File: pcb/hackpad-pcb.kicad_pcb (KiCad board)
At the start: 2 copper layers, 33 parts, among them U1 MCU_Seeed_XIAO_RP2040

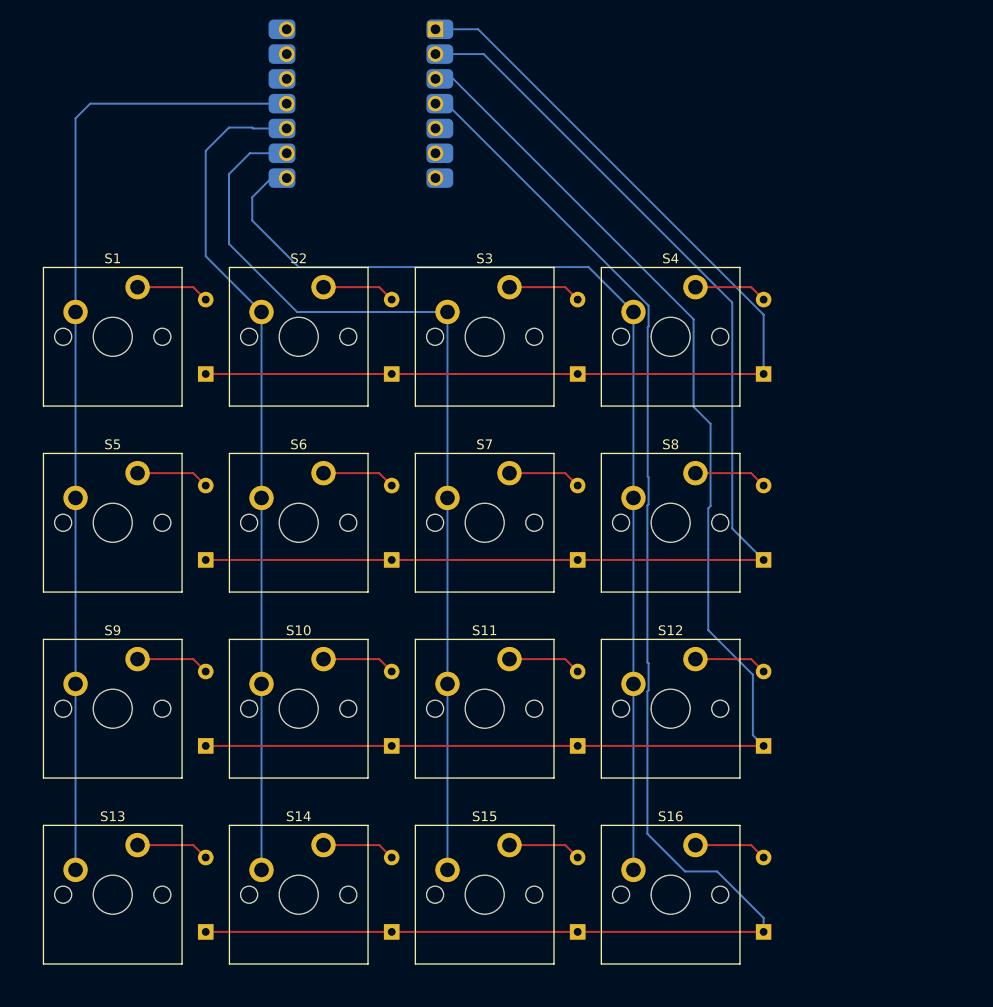
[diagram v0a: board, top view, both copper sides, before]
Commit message: Moved diodes and added OLED
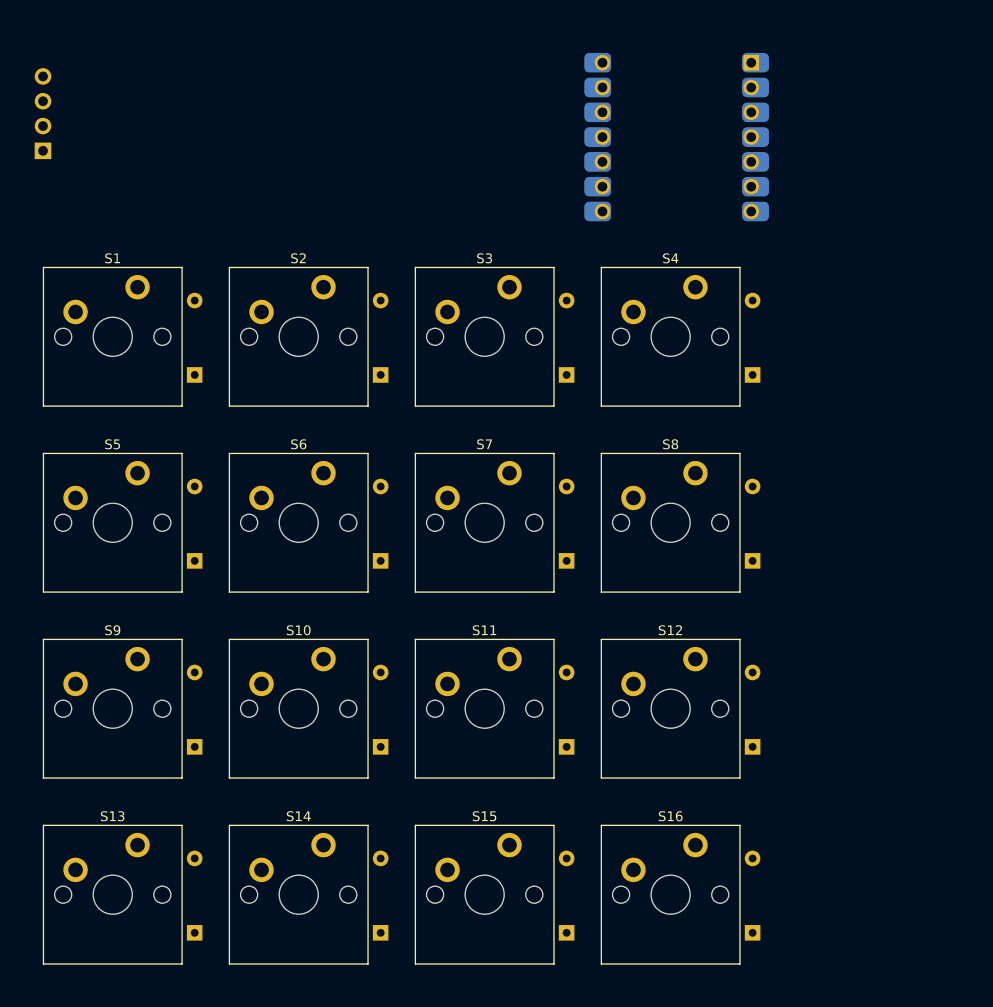
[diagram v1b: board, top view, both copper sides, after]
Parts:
- added J1: OLED_128x32, ScottoKeebs_Components:OLED_128x32, F.Cu at (105.6, 47.4)
- moved U1 32.5 mm to (172.1, 55.7)
- moved D11 1.14 mm to (160.8, 118.2)
- moved D15 1.14 mm to (160.8, 137.3)
- moved D3 1.14 mm to (160.8, 80.1)
- moved D7 1.14 mm to (160.8, 99.2)
- moved D1 1.14 mm to (122.7, 80.1)
- moved D13 1.14 mm to (122.7, 137.3)
- moved D5 1.14 mm to (122.7, 99.2)
- moved D9 1.14 mm to (122.7, 118.2)
- moved D10 1.14 mm to (141.7, 118.2)
- moved D12 1.14 mm to (179.8, 118.2)
- moved D14 1.14 mm to (141.7, 137.3)
- moved D16 1.14 mm to (179.8, 137.3)
- moved D2 1.14 mm to (141.7, 80.1)
- moved D4 1.14 mm to (179.8, 80.1)
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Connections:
- U1 pad 13: unconnected-(U1-GND-Pad13) -> GND
- U1 pad 14: unconnected-(U1-5V-Pad14) -> VCC
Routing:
- net Row 3: track 158.8 -> 0.00 mm
- net Row 2: track 140.2 -> 0.00 mm
- net Row 1: track 125.3 -> 0.00 mm
- net Row 0: track 108.9 -> 0.00 mm
- net Column 3: track 106.3 -> 0.00 mm
- net Column 0: track 98.8 -> 0.00 mm
- net Column 2: track 96.4 -> 0.00 mm
- net Column 1: track 84.9 -> 0.00 mm
- net Net-(D7-A): track 7.51 -> 0.00 mm
- net Net-(D6-A): track 7.51 -> 0.00 mm
- net Net-(D3-A): track 7.51 -> 0.00 mm
- net Net-(D2-A): track 7.51 -> 0.00 mm
- net Net-(D11-A): track 7.51 -> 0.00 mm
- net Net-(D10-A): track 7.51 -> 0.00 mm
- net Net-(D9-A): track 7.51 -> 0.00 mm
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
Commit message: Routed a little bit more
Signed-off-by: Urjith Mishra <66270347+TheScientist101@users.noreply.github.com>
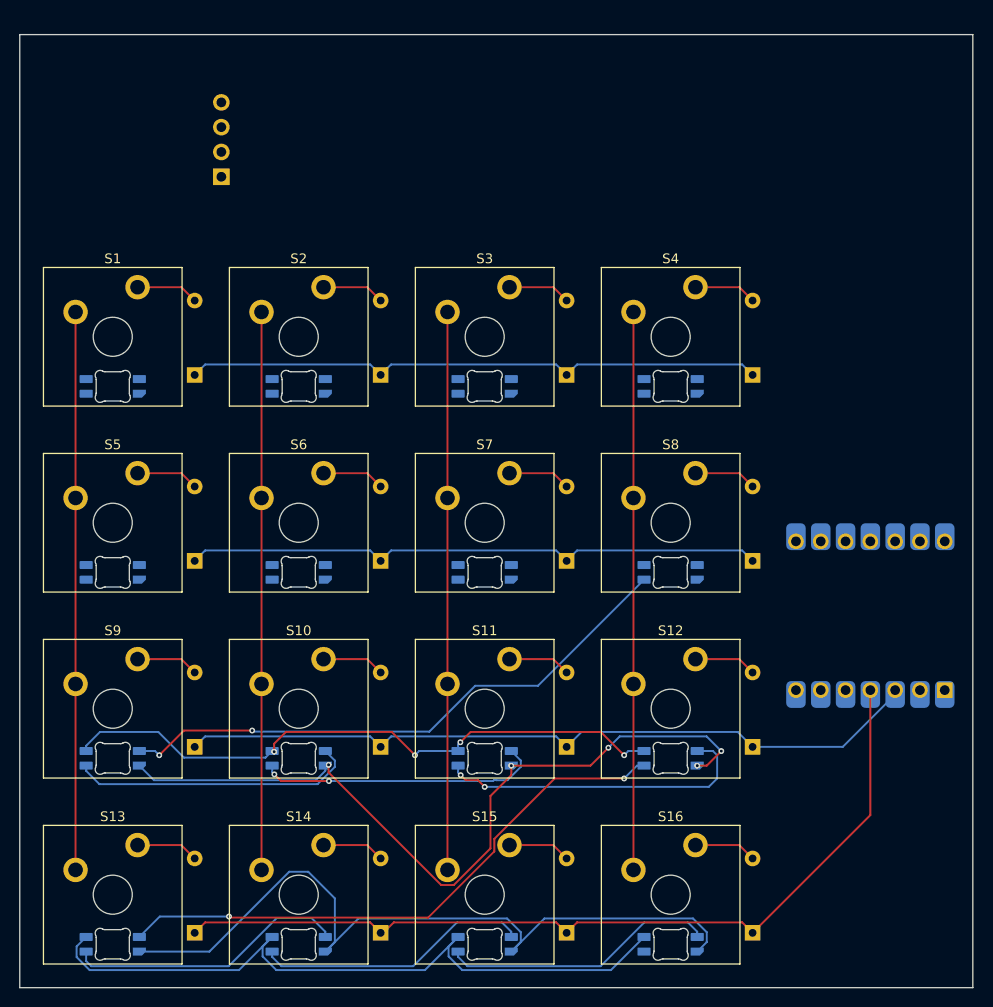
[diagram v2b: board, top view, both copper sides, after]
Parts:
- added LED1: MX_SK6812MINI-E, PCM_marbastlib-mx:LED_MX_6028R, B.Cu at (114.3, 81.3)
- added LED10: MX_SK6812MINI-E, PCM_marbastlib-mx:LED_MX_6028R, B.Cu at (133.3, 119.4)
- added LED11: MX_SK6812MINI-E, PCM_marbastlib-mx:LED_MX_6028R, B.Cu at (152.4, 119.4)
- added LED12: MX_SK6812MINI-E, PCM_marbastlib-mx:LED_MX_6028R, B.Cu at (171.4, 119.4)
- added LED13: MX_SK6812MINI-E, PCM_marbastlib-mx:LED_MX_6028R, B.Cu at (114.3, 138.4)
- added LED14: MX_SK6812MINI-E, PCM_marbastlib-mx:LED_MX_6028R, B.Cu at (133.3, 138.4)
- added LED15: MX_SK6812MINI-E, PCM_marbastlib-mx:LED_MX_6028R, B.Cu at (152.4, 138.4)
- added LED16: MX_SK6812MINI-E, PCM_marbastlib-mx:LED_MX_6028R, B.Cu at (171.4, 138.4)
- added LED2: MX_SK6812MINI-E, PCM_marbastlib-mx:LED_MX_6028R, B.Cu at (133.3, 81.3)
- added LED3: MX_SK6812MINI-E, PCM_marbastlib-mx:LED_MX_6028R, B.Cu at (152.4, 81.3)
- added LED4: MX_SK6812MINI-E, PCM_marbastlib-mx:LED_MX_6028R, B.Cu at (171.4, 81.3)
- added LED5: MX_SK6812MINI-E, PCM_marbastlib-mx:LED_MX_6028R, B.Cu at (114.3, 100.3)
- added LED6: MX_SK6812MINI-E, PCM_marbastlib-mx:LED_MX_6028R, B.Cu at (133.3, 100.3)
- added LED7: MX_SK6812MINI-E, PCM_marbastlib-mx:LED_MX_6028R, B.Cu at (152.4, 100.3)
- added LED8: MX_SK6812MINI-E, PCM_marbastlib-mx:LED_MX_6028R, B.Cu at (171.4, 100.3)
- added LED9: MX_SK6812MINI-E, PCM_marbastlib-mx:LED_MX_6028R, B.Cu at (114.3, 119.4)
- S1, S10, S11, S12, S13, S14, S15, S16, S2, S3, S4, S5, S6, S7, S8, S9: footprint ScottoKeebs_MX:MX_PCB_1.00u -> ScottoKeebs_MX:MX_Plate_1.00u
- moved U1 52.9 mm to (191.9, 104.8), turned to 90 degrees
- moved J1 18.5 mm to (123.8, 50.0)
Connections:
- J1 pad 3: unconnected-(J1-SCL-Pad3) -> /SCL
- J1 pad 4: unconnected-(J1-SDA-Pad4) -> /SDA
- U1 pad 5: unconnected-(U1-PA8_A4_D4_SDA-Pad5) -> /SDA
- U1 pad 6: unconnected-(U1-PA9_A5_D5_SCL-Pad6) -> /SCL
- U1 pad 7: unconnected-(U1-PB08_A6_D6_TX-Pad7) -> /LED Connector 0
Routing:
- net GND: track 0.00 -> 159.7 mm, vias 0 -> 5
- net VCC: track 0.00 -> 137.8 mm, vias 0 -> 4
- net Row 3: track 0.00 -> 89.7 mm
- net Row 2: track 0.00 -> 77.0 mm
- net /LED Connector 3: track 0.00 -> 59.8 mm, vias 0 -> 2
- net Row 0: track 0.00 -> 59.8 mm
- net Row 1: track 0.00 -> 59.8 mm
- net /LED Connector 2: track 0.00 -> 59.4 mm, vias 0 -> 2
- net Column 3: track 0.00 -> 57.2 mm
- net Column 2: track 0.00 -> 57.2 mm
- net Column 1: track 0.00 -> 57.2 mm
- net Column 0: track 0.00 -> 57.2 mm
- net Net-(LED11-DOUT): track 0.00 -> 32.8 mm, vias 0 -> 2
- net Net-(LED10-DIN): track 0.00 -> 30.1 mm
- net Net-(LED10-DOUT): track 0.00 -> 29.2 mm, vias 0 -> 2
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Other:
- board outline added: 97.6 x 97.6 mm

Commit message: Replaced neopixels with simple 2x3x4 mm leds to avoid smd soldering
Signed-off-by: Urjith Mishra <66270347+TheScientist101@users.noreply.github.com>
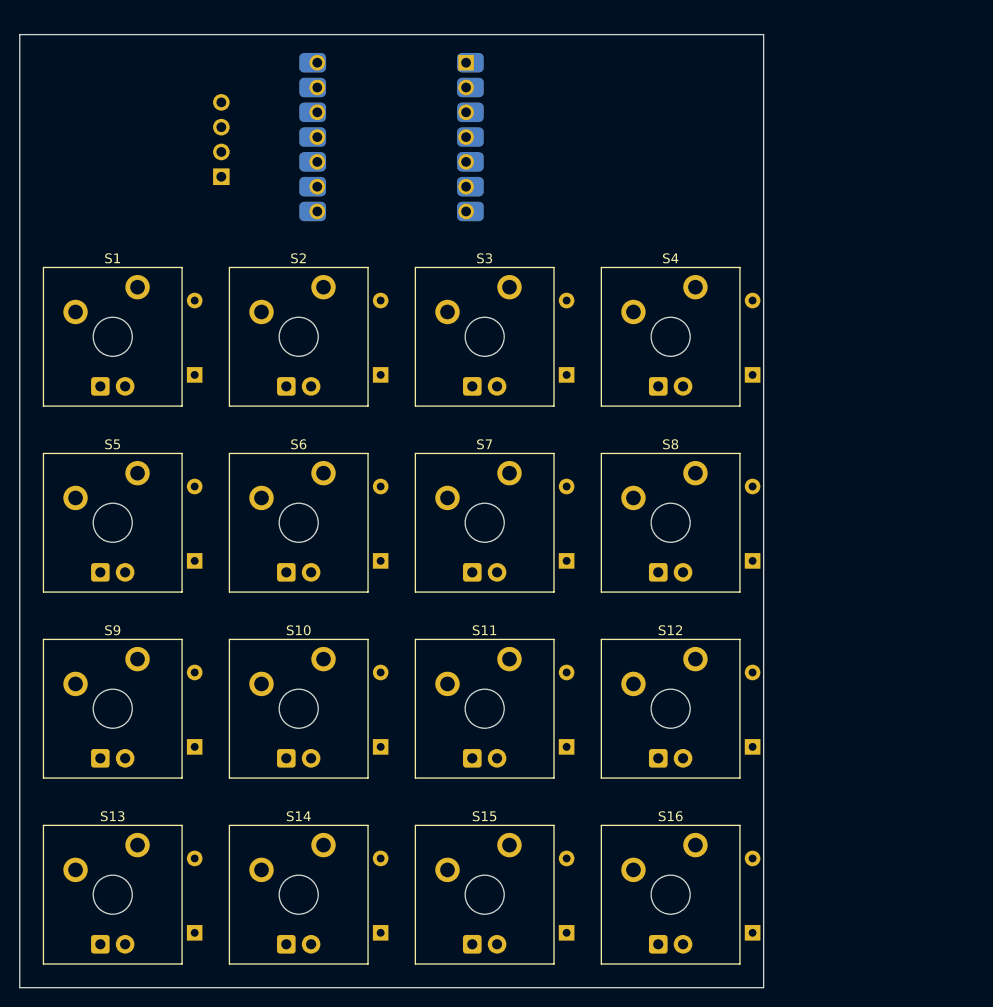
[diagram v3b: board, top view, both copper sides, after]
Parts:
- removed LED1, LED10, LED11, LED12, LED13, LED14, LED15, LED16, LED2, LED3, LED4, LED5, LED6, LED7, LED8, LED9: MX_SK6812MINI-E, PCM_marbastlib-mx:LED_MX_6028R
- added D17: LED, PCM_marbastlib-mx:LED_MX_3mm-ROT, F.Cu at (114.3, 81.3)
- added D18: LED, PCM_marbastlib-mx:LED_MX_3mm-ROT, F.Cu at (133.3, 81.3)
- added D19: LED, PCM_marbastlib-mx:LED_MX_3mm-ROT, F.Cu at (152.4, 81.3)
- added D20: LED, PCM_marbastlib-mx:LED_MX_3mm-ROT, F.Cu at (171.4, 81.3)
- added D21: LED, PCM_marbastlib-mx:LED_MX_3mm-ROT, F.Cu at (114.3, 100.3)
- added D22: LED, PCM_marbastlib-mx:LED_MX_3mm-ROT, F.Cu at (133.3, 100.3)
- added D23: LED, PCM_marbastlib-mx:LED_MX_3mm-ROT, F.Cu at (152.4, 100.3)
- added D24: LED, PCM_marbastlib-mx:LED_MX_3mm-ROT, F.Cu at (171.4, 100.3)
- added D25: LED, PCM_marbastlib-mx:LED_MX_3mm-ROT, F.Cu at (114.3, 119.4)
- added D26: LED, PCM_marbastlib-mx:LED_MX_3mm-ROT, F.Cu at (133.3, 119.4)
- added D27: LED, PCM_marbastlib-mx:LED_MX_3mm-ROT, F.Cu at (152.4, 119.4)
- added D28: LED, PCM_marbastlib-mx:LED_MX_3mm-ROT, F.Cu at (171.4, 119.4)
- added D29: LED, PCM_marbastlib-mx:LED_MX_3mm-ROT, F.Cu at (114.3, 138.4)
- added D30: LED, PCM_marbastlib-mx:LED_MX_3mm-ROT, F.Cu at (133.3, 138.4)
- added D31: LED, PCM_marbastlib-mx:LED_MX_3mm-ROT, F.Cu at (152.4, 138.4)
- added D32: LED, PCM_marbastlib-mx:LED_MX_3mm-ROT, F.Cu at (171.4, 138.4)
- moved U1 69.3 mm to (142.9, 55.7), turned to 180 degrees
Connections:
- U1 pad 12: unconnected-(U1-3V3-Pad12) -> +3V3
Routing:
- net GND: track 159.7 -> 0.00 mm, vias 5 -> 0
- net VCC: track 137.8 -> 0.00 mm, vias 4 -> 0
- net Row 3: track 89.7 -> 0.00 mm
- net Row 2: track 77.0 -> 0.00 mm
- net /LED Connector 3: track 59.8 -> 0.00 mm, vias 2 -> 0
- net Row 0: track 59.8 -> 0.00 mm
- net Row 1: track 59.8 -> 0.00 mm
- net /LED Connector 2: track 59.4 -> 0.00 mm, vias 2 -> 0
- net Column 3: track 57.2 -> 0.00 mm
- net Column 2: track 57.2 -> 0.00 mm
- net Column 1: track 57.2 -> 0.00 mm
- net Column 0: track 57.2 -> 0.00 mm
- net Net-(LED11-DOUT): track 32.8 -> 0.00 mm, vias 2 -> 0
- net Net-(LED10-DIN): track 30.1 -> 0.00 mm
- net Net-(LED10-DOUT): track 29.2 -> 0.00 mm, vias 2 -> 0
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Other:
- board size 97.6 x 97.6 mm -> 76.2 x 97.6 mm

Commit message: Routed pcb using freerouter
Signed-off-by: Urjith Mishra <66270347+TheScientist101@users.noreply.github.com>
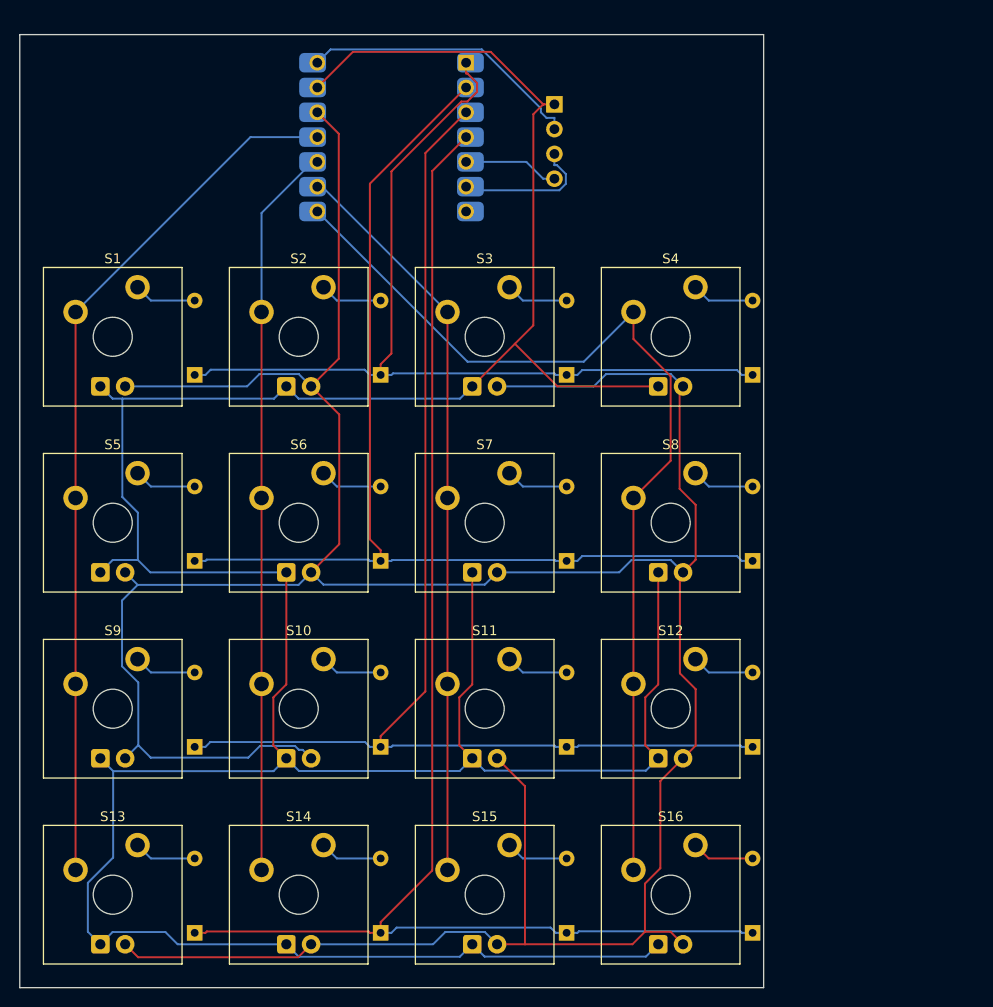
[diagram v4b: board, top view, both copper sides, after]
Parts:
- moved J1 39.3 mm to (161.1, 62.2), turned to 180 degrees
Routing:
- net GND: track 0.00 -> 354.8 mm
- net +3V3: track 0.00 -> 332.3 mm
- net Row 3: track 0.00 -> 143.4 mm
- net Row 2: track 0.00 -> 126.9 mm
- net Row 1: track 0.00 -> 111.2 mm
- net Column 3: track 0.00 -> 101.7 mm
- net Row 0: track 0.00 -> 95.6 mm
- net Column 0: track 0.00 -> 89.3 mm
- net Column 2: track 0.00 -> 76.3 mm
- net Column 1: track 0.00 -> 75.2 mm
- net VCC: track 0.00 -> 29.6 mm
- net /SCL: track 0.00 -> 14.4 mm
- net /SDA: track 0.00 -> 9.76 mm
- net Net-(D11-A): track 0.00 -> 6.42 mm
- net Net-(D10-A): track 0.00 -> 6.42 mm
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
